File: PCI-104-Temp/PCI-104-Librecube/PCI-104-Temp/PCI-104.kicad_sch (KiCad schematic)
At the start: 6 parts, among them J3 Conn_02x26_Row_Letter_First, J4 Conn_02x26_Row_Letter_First

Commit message: EPS PCB Ready for Order
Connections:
- net GND: now also J3.a17 (Pin_a17), J3.b17 (Pin_b17), J4.a15 (Pin_a15), J4.a16 (Pin_a16), J4.b15 (Pin_b15), J4.b16 (Pin_b16); no longer J3.a26 (Pin_a26), J3.b26 (Pin_b26), J4.a26 (Pin_a26)
- net ACDS_PWM_2: now reaches J3.a10 (Pin_a10)
- net ACDS_PWM_3: now reaches J3.a11 (Pin_a11)
- net ACDS_PWM_4: now reaches J3.a12 (Pin_a12)
- net 5V_PERM: now reaches J3.a13 (Pin_a13)
- net 5V_PERM: now also J3.b13 (Pin_b13), J4.a13 (Pin_a13), J4.b13 (Pin_b13)
- net ACDS_PERM_5: now reaches J3.a15 (Pin_a15)
- net ACDS_PERM_6: now reaches J3.a16 (Pin_a16)
- net RS SYS2 Rx: now reaches J3.a20 (Pin_a20)
- net STAT_2: now reaches J3.a5 (Pin_a5)
- net ACDS_PWM_1: now reaches J3.a9 (Pin_a9)
- net RS-485 SYS1 B: now reaches J3.b11 (Pin_b11)
- net RS-485 SYS1 B: now also J3.b12 (Pin_b12)
- net ACDS_IMU_RST: now reaches J3.b15 (Pin_b15)
- net RS SYS2 Tx: now reaches J3.b20 (Pin_b20)
- net UART_RX: now reaches J3.b21 (Pin_b21)
- net UART_TX: now reaches J3.b22 (Pin_b22)
- net ACDS_RS232_TX: now reaches J3.b3 (Pin_b3)
- net ACDS_RS232_RX: now reaches J3.b4 (Pin_b4)
- net PG: now reaches J3.b5 (Pin_b5)
- net INT: now reaches J3.b6 (Pin_b6)
- net STAT_1: now reaches J3.b7 (Pin_b7)
- net SDA: now reaches J3.b8 (Pin_b8)
- net SCL: now reaches J3.b9 (Pin_b9)
- net SUN_SENSE_1: now reaches J4.a1 (Pin_a1)
- net 12V: now reaches J4.a12 (Pin_a12)
- net 12V: now also J4.b12 (Pin_b12)
- net 3.3V: now reaches J4.a14 (Pin_a14)
- net 3.3V: now also J4.b14 (Pin_b14)
- net SUN_SENSE_3: now reaches J4.a2 (Pin_a2)
- net SOL_PIN: now reaches J4.a22 (Pin_a22)
- net SOL_PIN: now also J4.b22 (Pin_b22)
- net BATT_PIN: now reaches J4.a23 (Pin_a23)
- net BATT_PIN: now also J4.a24 (Pin_a24)
- net RBF_A: now reaches J4.a25 (Pin_a25)
- net THR_1: now reaches J4.a3 (Pin_a3)
- net THR_3: now reaches J4.a4 (Pin_a4)
- net SUN_SENSE_2: now reaches J4.b1 (Pin_b1)
- net HEATER_PWM: now reaches J4.b10 (Pin_b10)
- net SUN_SENSE_4: now reaches J4.b2 (Pin_b2)
- net SYS_PIN: now reaches J4.b23 (Pin_b23)
- net SYS_PIN: now also J4.b24 (Pin_b24)
- net RBF_B: now reaches J4.b25 (Pin_b25)
- net DS_B: now reaches J4.b26 (Pin_b26)
- net THR_2: now reaches J4.b3 (Pin_b3)
- net THR_4: now reaches J4.b4 (Pin_b4)
- net THR_5: now reaches J4.b5 (Pin_b5)
- net THR_6: now reaches J4.b6 (Pin_b6)
- net THR_7: now reaches J4.b7 (Pin_b7)
- net THR_8: now reaches J4.b8 (Pin_b8)
- net THR_9: now reaches J4.b9 (Pin_b9)
- new net DS_A: J4.a26 (Pin_a26)
- no-connect marks 0 -> 42
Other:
- moved on the sheet: H1, H2, H3, H4, J4

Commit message: Small PC104 Template Fix
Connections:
- net RS-485 SYS1 B: no longer J3.b12 (Pin_b12)
- new net RS-485 SYS1 A: J3.b12 (Pin_b12)
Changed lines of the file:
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@@
 		)
 	)
-	(global_label "RS-485 SYS1 B"
+	(global_label "RS-485 SYS1 A"
 		(shape input)
 		(at 182.88 82.55 0)
@@
 		)
 		(property "Intersheetrefs" "${INTERSHEET_REFS}"
-			(at 201.4679 82.55 0)
+			(at 201.2865 82.55 0)
 			(hide yes)
 			(show_name no)

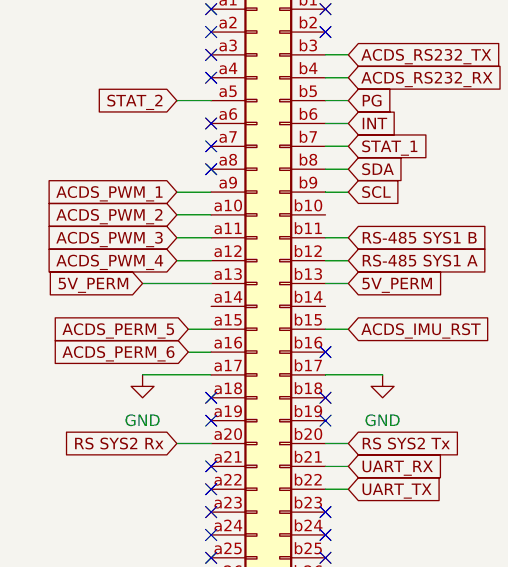
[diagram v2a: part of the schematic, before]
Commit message: updated PC104 ADCS pins
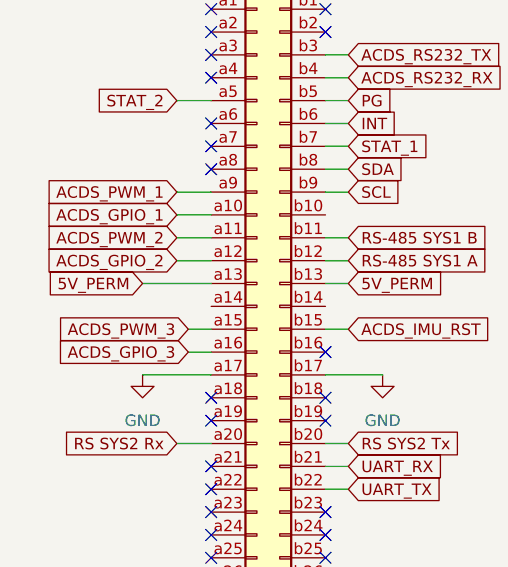
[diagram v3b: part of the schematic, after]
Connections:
- net ACDS_PERM_5 is gone; now on net ACDS_PWM_3: J3.a15 (Pin_a15)
- net ACDS_PWM_2: now also J3.a11 (Pin_a11); no longer J3.a10 (Pin_a10)
- net ACDS_PWM_3: no longer J3.a11 (Pin_a11)
- net ACDS_PERM_6 renamed ACDS_GPIO_3
- net ACDS_PWM_4 renamed ACDS_GPIO_2
- new net ACDS_GPIO_1: J3.a10 (Pin_a10)
